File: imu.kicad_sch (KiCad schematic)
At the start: 9 parts, among them U2 MPU-6500

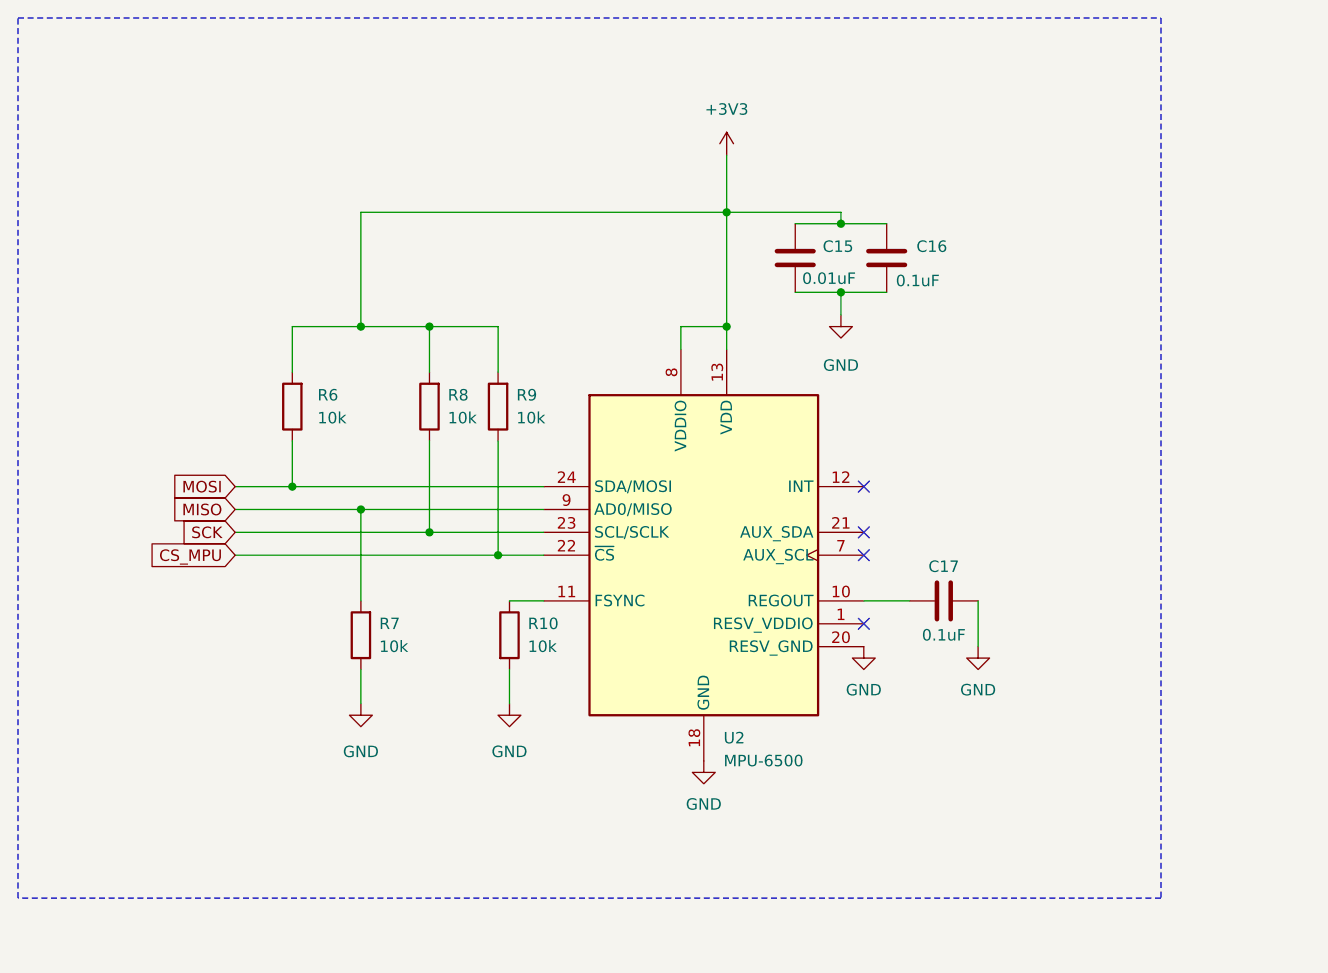
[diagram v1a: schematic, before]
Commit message: Add files via upload
Added hivoltage cirquit. TODO - add powon (VT19 on MSX)
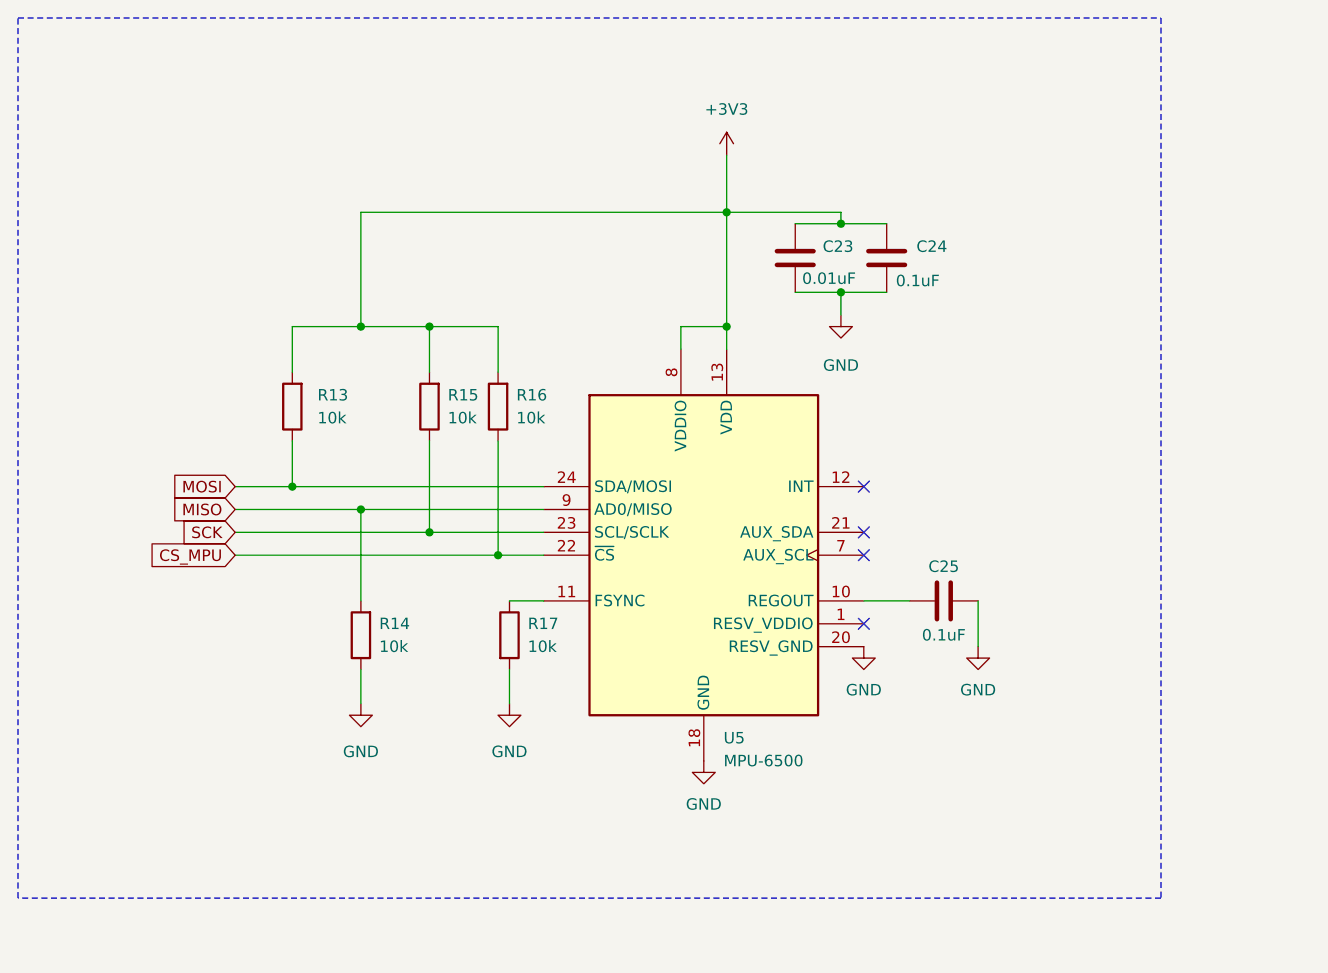
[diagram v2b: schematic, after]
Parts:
- renumbered C15 to C23, C16 to C24, C17 to C25, R6 to R13, R7 to R14, R8 to R15, R9 to R16, R10 to R17, U2 to U5
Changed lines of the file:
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@@
   (symbol (lib_id "Device:R") (at 127 113.03 0) (unit 1)
     (in_bom yes) (on_board yes) (dnp no)
-    (property "Reference" "R10" (at 129.032 111.7599 0)
+    (property "Reference" "R17" (at 129.032 111.7599 0)
       (effects (font (size 1.27 1.27)) (justify left))
     )
@@
       (project "ShiftWay_f103"
         (path "/c57bc97c-1c43-4bb1-9424-fed846030b7b/44aacc1d-3f92-4714-b852-d77f581a6611"
-          (reference "R10") (unit 1)
+          (reference "R17") (unit 1)
         )
       )
@@
   (symbol (lib_id "power:GND") (at 166.37 114.3 0) (unit 1)
     (in_bom yes) (on_board yes) (dnp no) (fields_autoplaced)
-    (property "Reference" "#PWR031" (at 166.37 120.65 0)
+    (property "Reference" "#PWR047" (at 166.37 120.65 0)
       (effects (font (size 1.27 1.27)) hide)
     )
@@
       (project "ShiftWay_f103"
         (path "/c57bc97c-1c43-4bb1-9424-fed846030b7b/44aacc1d-3f92-4714-b852-d77f581a6611"
-          (reference "#PWR031") (unit 1)
+          (reference "#PWR047") (unit 1)
         )
       )
@@
   (symbol (lib_id "power:GND") (at 110.49 120.65 0) (unit 1)
     (in_bom yes) (on_board yes) (dnp no) (fields_autoplaced)
-    (property "Reference" "#PWR026" (at 110.49 127 0)
+    (property "Reference" "#PWR042" (at 110.49 127 0)
       (effects (font (size 1.27 1.27)) hide)
     )
@@
       (project "ShiftWay_f103"
         (path "/c57bc97c-1c43-4bb1-9424-fed846030b7b/44aacc1d-3f92-4714-b852-d77f581a6611"
-          (reference "#PWR026") (unit 1)
+          (reference "#PWR042") (unit 1)
         )
       )
@@
   (symbol (lib_id "power:+3V3") (at 151.13 59.69 0) (unit 1)
     (in_bom yes) (on_board yes) (dnp no) (fields_autoplaced)
-    (property "Reference" "#PWR029" (at 151.13 63.5 0)
+    (property "Reference" "#PWR045" (at 151.13 63.5 0)
       (effects (font (size 1.27 1.27)) hide)
     )
@@
       (project "ShiftWay_f103"
         (path "/c57bc97c-1c43-4bb1-9424-fed846030b7b/44aacc1d-3f92-4714-b852-d77f581a6611"
-          (reference "#PWR029") (unit 1)
+          (reference "#PWR045") (unit 1)
         )
       )
@@
   (symbol (lib_id "power:GND") (at 148.59 127 0) (unit 1)
     (in_bom yes) (on_board yes) (dnp no) (fields_autoplaced)
-    (property "Reference" "#PWR028" (at 148.59 133.35 0)
+    (property "Reference" "#PWR044" (at 148.59 133.35 0)
       (effects (font (size 1.27 1.27)) hide)
     )
@@
       (project "ShiftWay_f103"
         (path "/c57bc97c-1c43-4bb1-9424-fed846030b7b/44aacc1d-3f92-4714-b852-d77f581a6611"
-          (reference "#PWR028") (unit 1)
+          (reference "#PWR044") (unit 1)
         )
       )
@@
   (symbol (lib_id "Device:C") (at 168.91 71.12 0) (unit 1)
     (in_bom yes) (on_board yes) (dnp no)
-    (property "Reference" "C16" (at 172.212 69.8499 0)
+    (property "Reference" "C24" (at 172.212 69.8499 0)
       (effects (font (size 1.27 1.27)) (justify left))
     )
@@
       (project "ShiftWay_f103"
         (path "/c57bc97c-1c43-4bb1-9424-fed846030b7b/44aacc1d-3f92-4714-b852-d77f581a6611"
-          (reference "C16") (unit 1)
+          (reference "C24") (unit 1)
         )
       )
@@
   (symbol (lib_id "power:GND") (at 163.83 77.47 0) (unit 1)
     (in_bom yes) (on_board yes) (dnp no) (fields_autoplaced)
-    (property "Reference" "#PWR030" (at 163.83 83.82 0)
+    (property "Reference" "#PWR046" (at 163.83 83.82 0)
       (effects (font (size 1.27 1.27)) hide)
     )
@@
       (project "ShiftWay_f103"
         (path "/c57bc97c-1c43-4bb1-9424-fed846030b7b/44aacc1d-3f92-4714-b852-d77f581a6611"
-          (reference "#PWR030") (unit 1)
+          (reference "#PWR046") (unit 1)
         )
       )
@@
   (symbol (lib_id "Device:R") (at 118.11 87.63 180) (unit 1)
     (in_bom yes) (on_board yes) (dnp no) (fields_autoplaced)
-    (property "Reference" "R8" (at 120.142 86.3599 0)
+    (property "Reference" "R15" (at 120.142 86.3599 0)
       (effects (font (size 1.27 1.27)) (justify right))
     )
@@
       (project "ShiftWay_f103"
         (path "/c57bc97c-1c43-4bb1-9424-fed846030b7b/44aacc1d-3f92-4714-b852-d77f581a6611"
-          (reference "R8") (unit 1)
+          (reference "R15") (unit 1)
         )
       )
@@
   (symbol (lib_id "power:GND") (at 179.07 114.3 0) (unit 1)
     (in_bom yes) (on_board yes) (dnp no) (fields_autoplaced)
-    (property "Reference" "#PWR032" (at 179.07 120.65 0)
+    (property "Reference" "#PWR048" (at 179.07 120.65 0)
       (effects (font (size 1.27 1.27)) hide)
     )
@@
       (project "ShiftWay_f103"
         (path "/c57bc97c-1c43-4bb1-9424-fed846030b7b/44aacc1d-3f92-4714-b852-d77f581a6611"
-          (reference "#PWR032") (unit 1)
+          (reference "#PWR048") (unit 1)
         )
       )
@@
   (symbol (lib_id "Device:R") (at 110.49 113.03 180) (unit 1)
     (in_bom yes) (on_board yes) (dnp no) (fields_autoplaced)
-    (property "Reference" "R7" (at 112.522 111.7599 0)
+    (property "Reference" "R14" (at 112.522 111.7599 0)
       (effects (font (size 1.27 1.27)) (justify right))
     )
@@
       (project "ShiftWay_f103"
         (path "/c57bc97c-1c43-4bb1-9424-fed846030b7b/44aacc1d-3f92-4714-b852-d77f581a6611"
-          (reference "R7") (unit 1)
+          (reference "R14") (unit 1)
         )
       )
@@
   (symbol (lib_id "Device:R") (at 102.87 87.63 180) (unit 1)
     (in_bom yes) (on_board yes) (dnp no) (fields_autoplaced)
-    (property "Reference" "R6" (at 105.664 86.3599 0)
+    (property "Reference" "R13" (at 105.664 86.3599 0)
       (effects (font (size 1.27 1.27)) (justify right))
     )
@@
       (project "ShiftWay_f103"
         (path "/c57bc97c-1c43-4bb1-9424-fed846030b7b/44aacc1d-3f92-4714-b852-d77f581a6611"
-          (reference "R6") (unit 1)
+          (reference "R13") (unit 1)
         )
       )
@@
   (symbol (lib_id "power:GND") (at 127 120.65 0) (unit 1)
     (in_bom yes) (on_board yes) (dnp no) (fields_autoplaced)
-    (property "Reference" "#PWR027" (at 127 127 0)
+    (property "Reference" "#PWR043" (at 127 127 0)
       (effects (font (size 1.27 1.27)) hide)
     )
@@
       (project "ShiftWay_f103"
         (path "/c57bc97c-1c43-4bb1-9424-fed846030b7b/44aacc1d-3f92-4714-b852-d77f581a6611"
-          (reference "#PWR027") (unit 1)
+          (reference "#PWR043") (unit 1)
         )
       )
@@
   (symbol (lib_id "Device:C") (at 175.26 109.22 270) (unit 1)
     (in_bom yes) (on_board yes) (dnp no)
-    (property "Reference" "C17" (at 175.26 105.41 90)
+    (property "Reference" "C25" (at 175.26 105.41 90)
       (effects (font (size 1.27 1.27)))
     )
@@
       (project "ShiftWay_f103"
         (path "/c57bc97c-1c43-4bb1-9424-fed846030b7b/44aacc1d-3f92-4714-b852-d77f581a6611"
-          (reference "C17") (unit 1)
+          (reference "C25") (unit 1)
         )
       )
@@
   (symbol (lib_id "Sensor_Motion:MPU-9250") (at 148.59 104.14 0) (unit 1)
     (in_bom yes) (on_board yes) (dnp no) (fields_autoplaced)
-    (property "Reference" "U2" (at 150.7841 124.46 0)
+    (property "Reference" "U5" (at 150.7841 124.46 0)
       (effects (font (size 1.27 1.27)) (justify left))
     )
@@
       (project "ShiftWay_f103"
         (path "/c57bc97c-1c43-4bb1-9424-fed846030b7b/44aacc1d-3f92-4714-b852-d77f581a6611"
-          (reference "U2") (unit 1)
+          (reference "U5") (unit 1)
         )
       )
@@
   (symbol (lib_id "Device:R") (at 125.73 87.63 180) (unit 1)
     (in_bom yes) (on_board yes) (dnp no) (fields_autoplaced)
-    (property "Reference" "R9" (at 127.762 86.3599 0)
+    (property "Reference" "R16" (at 127.762 86.3599 0)
       (effects (font (size 1.27 1.27)) (justify right))
     )
@@
       (project "ShiftWay_f103"
         (path "/c57bc97c-1c43-4bb1-9424-fed846030b7b/44aacc1d-3f92-4714-b852-d77f581a6611"
-          (reference "R9") (unit 1)
+          (reference "R16") (unit 1)
         )
       )
@@
   (symbol (lib_id "Device:C") (at 158.75 71.12 0) (unit 1)
     (in_bom yes) (on_board yes) (dnp no)
-    (property "Reference" "C15" (at 161.798 69.8499 0)
+    (property "Reference" "C23" (at 161.798 69.8499 0)
       (effects (font (size 1.27 1.27)) (justify left))
     )
@@
       (project "ShiftWay_f103"
         (path "/c57bc97c-1c43-4bb1-9424-fed846030b7b/44aacc1d-3f92-4714-b852-d77f581a6611"
-          (reference "C15") (unit 1)
-        )
-      )
+          (reference "C23") (unit 1)
+        )
+      )

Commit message: Divider, gate, mtr button, testpoints, minors
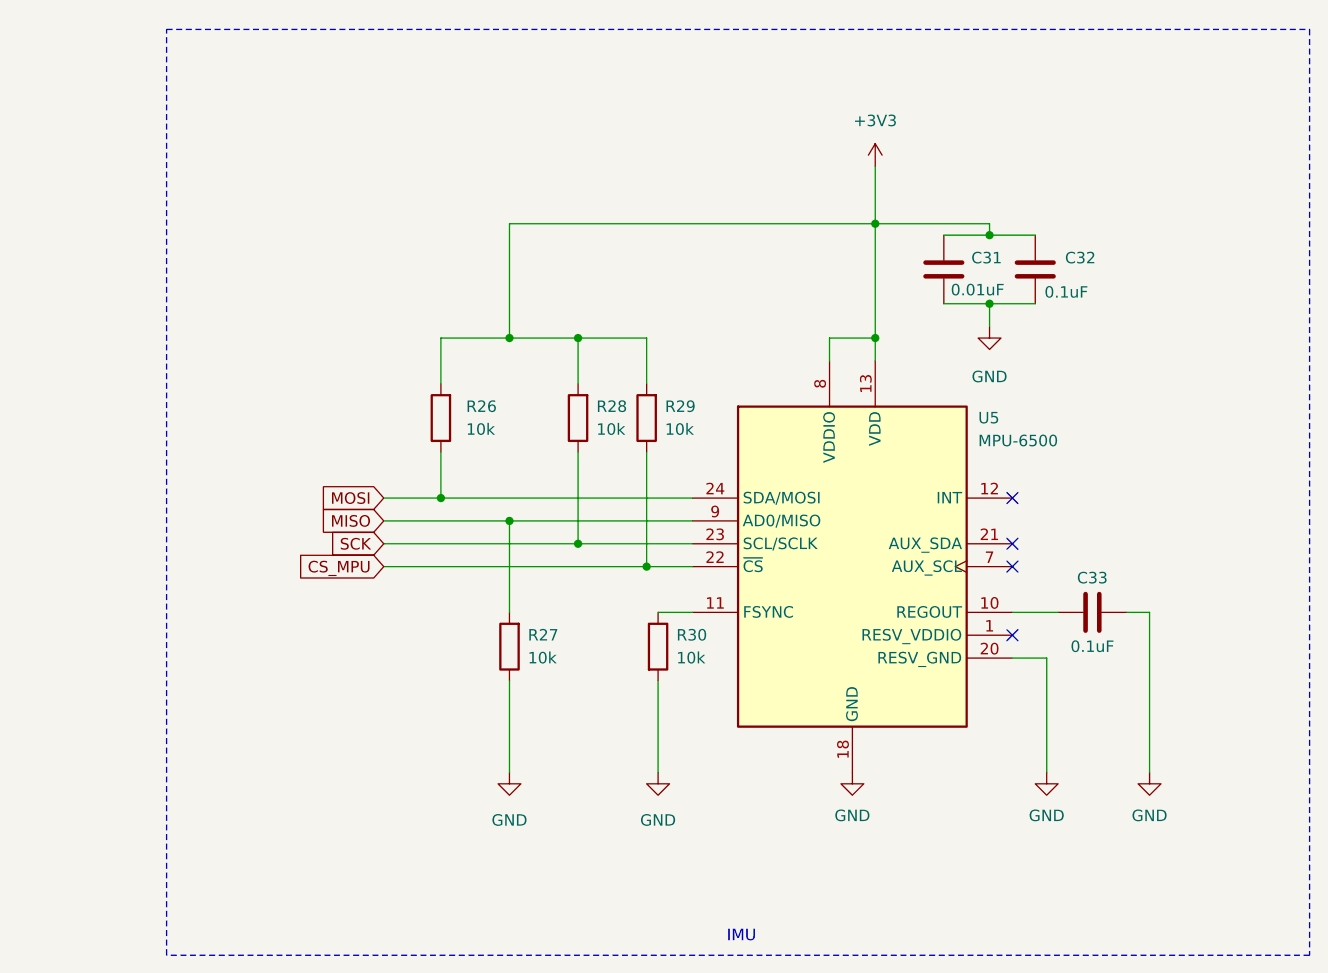
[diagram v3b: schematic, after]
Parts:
- renumbered C23 to C31, C24 to C32, C25 to C33, R13 to R26, R14 to R27, R15 to R28, R16 to R29, R17 to R30
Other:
- note added: "IMU"
- moved on the sheet: C31, C32, C33, R26, R27, R28, R29, R30, U5

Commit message: Minors, annotation
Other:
- title: (none) -> RedShift-117.6-LogicBoard-F103
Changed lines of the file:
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@@
 (kicad_sch (version 20230121) (generator eeschema)
   (paper "A4")
+  (title_block
+    (title "RedShift-117.6-LogicBoard-F103")
+    (date "08.12.2023")
+    (rev "0.1")
+  )
   (junction (at 180.34 68.58) (diameter 0) (color 0 0 0 0)
   )

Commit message: Add footprints, fixed xtal
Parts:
- C33: renamed from C31; footprint Capacitor_SMD:C_0402_1005Metric -> Capacitor_SMD:C_0603_1608Metric_Pad1.08x0.95mm_HandSolder
- C34: renamed from C32; footprint Capacitor_SMD:C_0402_1005Metric -> Capacitor_SMD:C_0603_1608Metric_Pad1.08x0.95mm_HandSolder
- C35: renamed from C33; footprint Capacitor_SMD:C_0402_1005Metric -> Capacitor_SMD:C_0603_1608Metric_Pad1.08x0.95mm_HandSolder
- R27: renamed from R26; footprint Resistor_SMD:R_0402_1005Metric -> Resistor_SMD:R_0603_1608Metric_Pad0.98x0.95mm_HandSolder
- R28: renamed from R27; footprint Resistor_SMD:R_0402_1005Metric -> Resistor_SMD:R_0603_1608Metric_Pad0.98x0.95mm_HandSolder
- R29: renamed from R28; footprint Resistor_SMD:R_0402_1005Metric -> Resistor_SMD:R_0603_1608Metric_Pad0.98x0.95mm_HandSolder
- R30: renamed from R29; footprint Resistor_SMD:R_0402_1005Metric -> Resistor_SMD:R_0603_1608Metric_Pad0.98x0.95mm_HandSolder
- R31: renamed from R30; footprint Resistor_SMD:R_0402_1005Metric -> Resistor_SMD:R_0603_1608Metric_Pad0.98x0.95mm_HandSolder
